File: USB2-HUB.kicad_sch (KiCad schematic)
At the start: 42 parts, among them J4 USB_OTG, U2 TLV71311PDBV, U3 FSUSB42MUX, U4 TUSB4041IPAPQ1, U5 TPD4EUSB30, Y1 24MHz Crystal

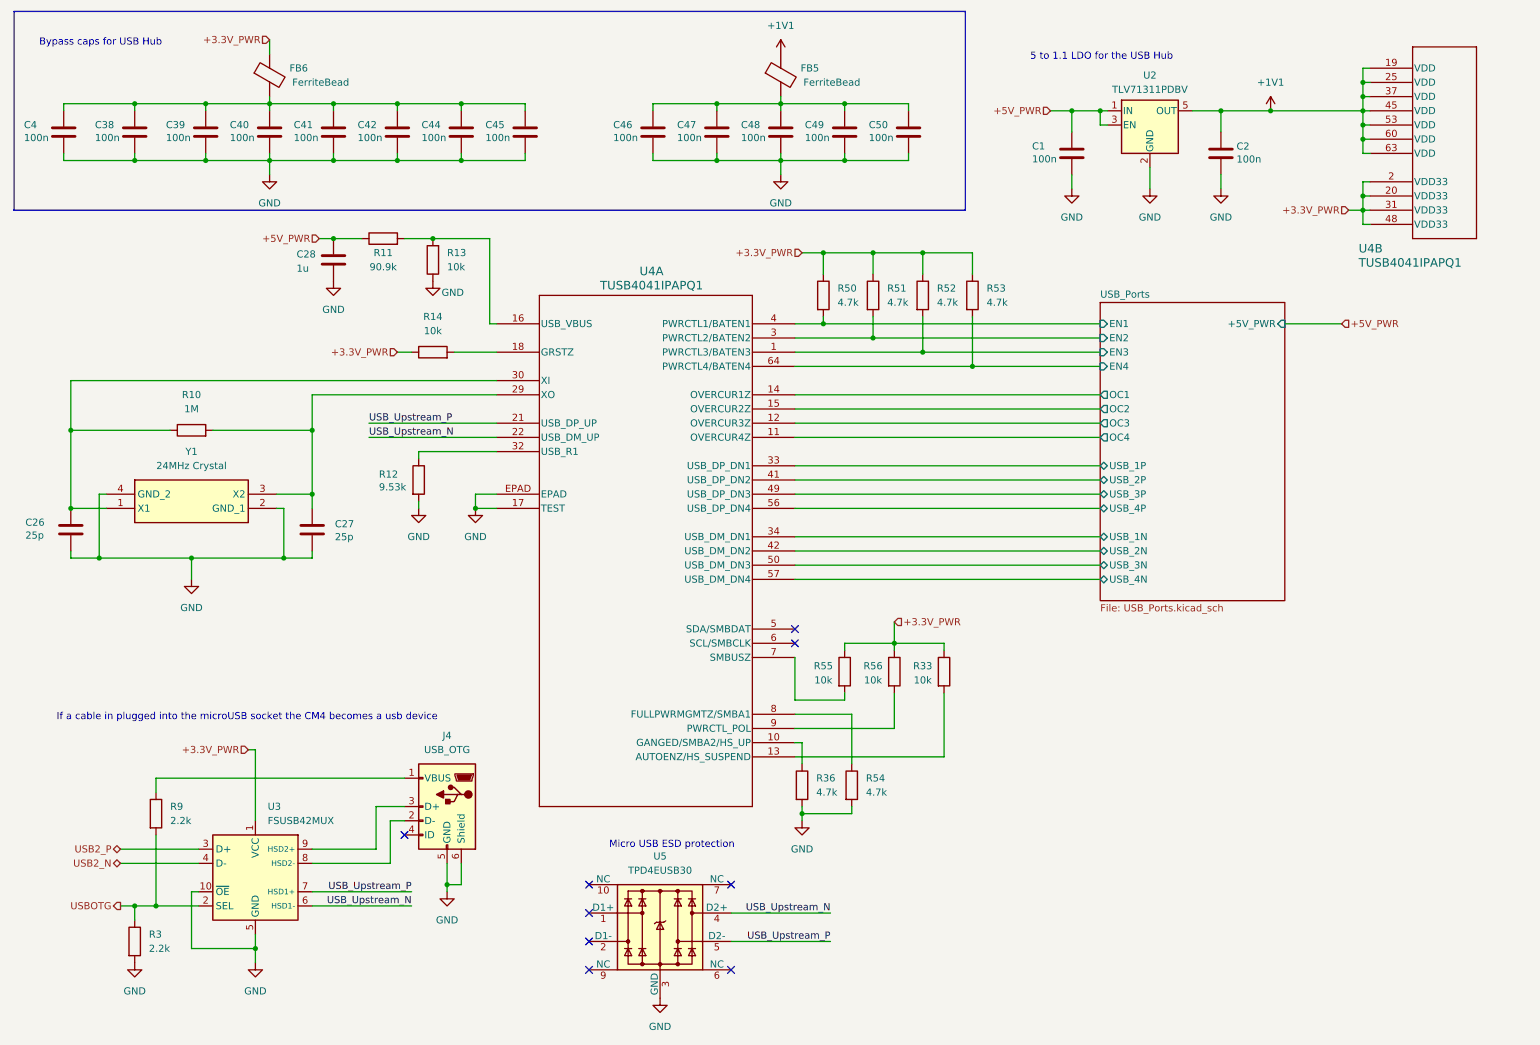
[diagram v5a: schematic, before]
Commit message: Migrate to USB C and added some ESD protections on Vbus; might still have some issues
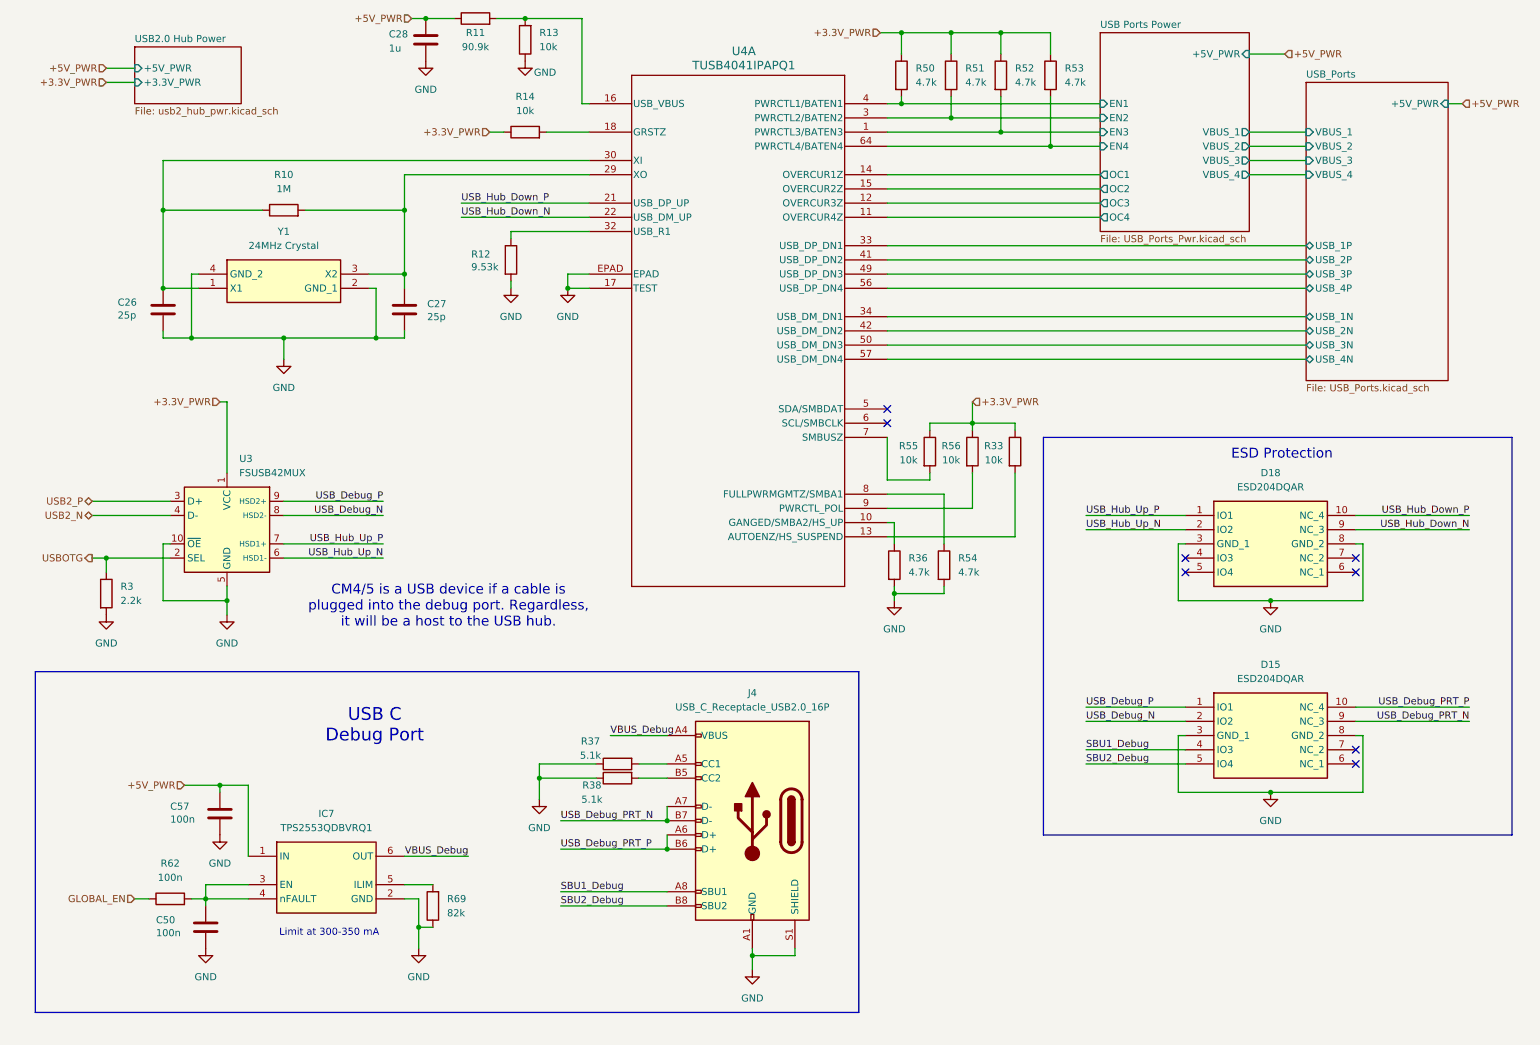
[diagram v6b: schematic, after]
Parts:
- removed C1, C2, C38, C39, C4, C40, C41, C42, C44, C45, C46, C47, C48, C49: 100n, Capacitor_SMD:C_0805_2012Metric, symbol Device:C
- removed FB5, FB6: FerriteBead, Inductor_SMD:L_1206_3216Metric, symbol Device:FerriteBead
- removed J4: USB_OTG, Connector_USB:USB_Micro-B_Molex-105017-0001, symbol Connector:USB_OTG
- removed R9: 2.2k, Resistor_SMD:R_0805_2012Metric, symbol Device:R
- removed U2: TLV71311PDBV, Package_TO_SOT_SMD:SOT-23-5, symbol Regulator_Linear:TLV71311PDBV
- removed unit 2 of U4
- removed U5: TPD4EUSB30, Package_SON:USON-10_2.5x1.0mm_P0.5mm, symbol Power_Protection:TPD4EUSB30
- added C57: 100n, Capacitor_SMD:C_0805_2012Metric, symbol Device:C
- added D15, D18: ESD204DQAR, Controls_Pi:ESD204DQAR, symbol ESD204DQAR:ESD204DQAR
- added IC7: TPS2553QDBVRQ1, Controls_Pi:SOT95P280X145-6N, symbol TPS2553QDBVRQ1:TPS2553QDBVRQ1
- added J4: USB_C_Receptacle_USB2.0_16P, symbol Connector:USB_C_Receptacle_USB2.0_16P
- added R37, R38: 5.1k, Resistor_SMD:R_0805_2012Metric, symbol Device:R
- added R62: 100n, Resistor_SMD:R_0805_2012Metric, symbol Device:R
- added R69: 82k, Resistor_SMD:R_0805_2012Metric, symbol Device:R
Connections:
- net +5V_PWR: now also C57.1, IC7.1 (IN)
- net GND: now also C57.2, D15.3 (GND_1), D15.8 (GND_2), D18.3 (GND_1), D18.8 (GND_2), IC7.2 (GND), J4.A1 (GND), J4.A12 (GND), J4.B1 (GND), J4.B12 (GND), J4.S1 (SHIELD), R37.1, R38.1, R69.1
- net at C50.1: now also IC7.3 (EN), IC7.4 (nFAULT), R62.2
- net USB_Debug_N: now reaches U3.8 (HSD2-)
- net USB_Debug_N: now also D15.2 (IO2)
- net USB_Debug_P: now reaches U3.9 (HSD2+)
- net USB_Debug_P: now also D15.1 (IO1)
- net USB_Ports/EN1 renamed USB Ports Power/EN1
- net USB_Ports/EN2 renamed USB Ports Power/EN2
- net USB_Ports/EN3 renamed USB Ports Power/EN3
- net USB_Ports/EN4 renamed USB Ports Power/EN4
- net USB_Ports/OC1 renamed USB Ports Power/OC1
- net USB_Ports/OC2 renamed USB Ports Power/OC2
- net USB_Ports/OC3 renamed USB Ports Power/OC3
- net USB_Ports/OC4 renamed USB Ports Power/OC4
- net USB_Upstream_N renamed USB_Hub_Down_N
- net USB_Hub_Down_N: now also D18.9 (NC_3); no longer U3.6 (HSD1-)
- net USB_Upstream_P renamed USB_Hub_Down_P
- net USB_Hub_Down_P: now also D18.10 (NC_4); no longer U3.7 (HSD1+)
- new net: J4.A5 (CC1), R37.2
- new net: IC7.5 (ILIM), R69.2
- new net: J4.B5 (CC2), R38.2
- new net GLOBAL_EN: R62.1
- new net SBU1_Debug: D15.4 (IO3), J4.A8 (SBU1)
- new net SBU2_Debug: D15.5 (IO4), J4.B8 (SBU2)
- new net USB_Debug_PRT_N: D15.9 (NC_3), J4.A7 (D-), J4.B7 (D-)
- new net USB_Debug_PRT_P: D15.10 (NC_4), J4.A6 (D+), J4.B6 (D+)
- new net USB_Hub_Up_N: D18.2 (IO2), U3.6 (HSD1-)
- new net USB_Hub_Up_P: D18.1 (IO1), U3.7 (HSD1+)
- new net VBUS_Debug: IC7.6 (OUT), J4.A4 (VBUS), J4.A9 (VBUS), J4.B4 (VBUS), J4.B9 (VBUS)
- no-connect marks 9 -> 8
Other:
- added sheet USB Ports Power (USB_Ports_Pwr.kicad_sch)
- added sheet USB2.0 Hub Power (usb2_hub_pwr.kicad_sch)
- sheet USB_Ports ports: added VBUS_1, VBUS_2, VBUS_3, VBUS_4; removed EN1, EN2, EN3, EN4, OC1, OC2, OC3, OC4
- note added: "CM4/5 is a USB device if a cable is plugged into the debug port. Regardless, it will be a host to the USB hub."
- note added: "ESD Protection"
- note added: "Limit at 300-350 mA"
- note added: "USB C Debug Port"
- note removed: "5 to 1.1 LDO for the USB Hub"
- note removed: "Bypass caps for USB Hub"
- note removed: "If a cable in plugged into the microUSB socket the CM4 becomes a usb device"
- note removed: "Micro USB ESD protection"
- moved on the sheet: C26, C27, C28, R10, R11, R12, R13, R14, R3, R33, R36, R50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

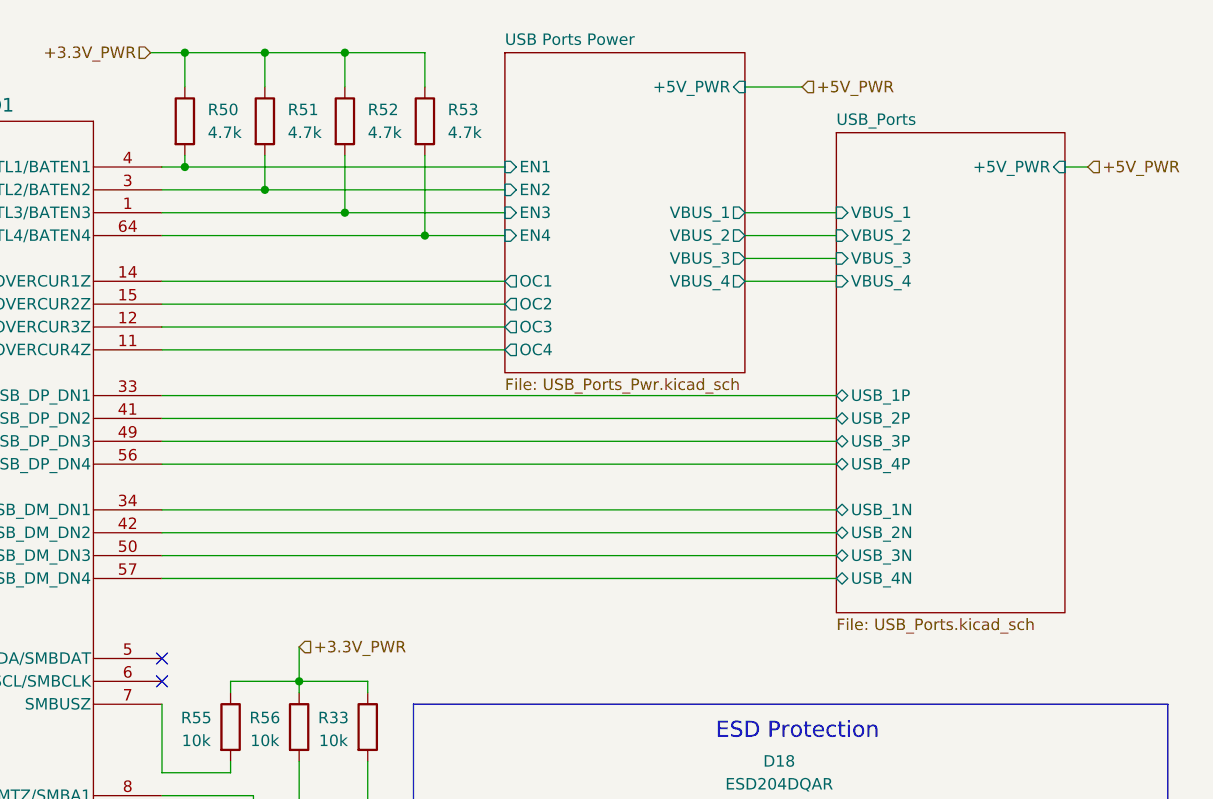
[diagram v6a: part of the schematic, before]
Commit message: fixed erc and removed old schematics
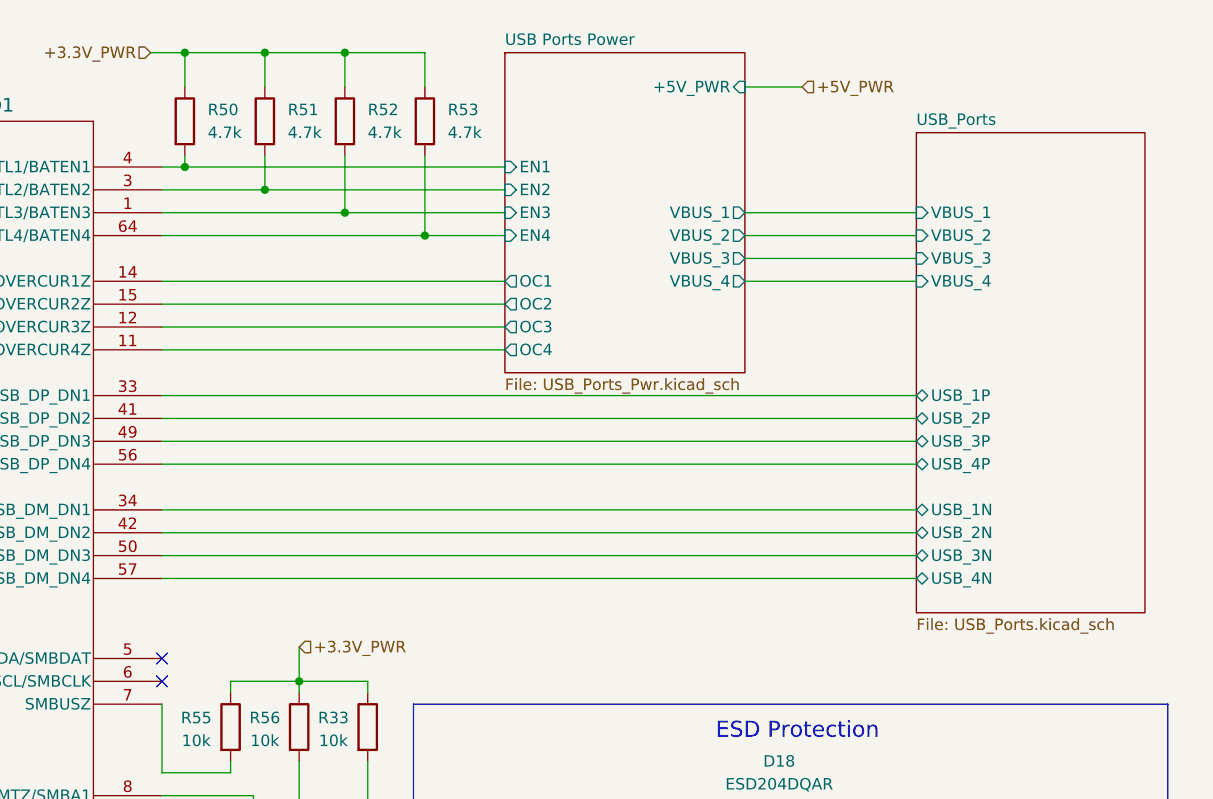
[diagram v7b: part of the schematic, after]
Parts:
- D15, D18: Arrow Part Number (none) -> ESD204DQAR; Arrow Price/Stock (none) -> https://www.arrow.com/en/products/esd204dqar/texas-instrume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; Height (none) -> 0.55; Manufacturer_Name (none) -> Texas Instruments; Manufacturer_Part_Number (none) -> ESD204DQAR; Mouser Part Number (none) -> 595-ESD204DQAR; Mouser Price/Stock (none) -> https://www.mouser.co.uk/ProductDetail/Texas-Instruments/ES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
- IC7: Arrow Part Number (none) -> TPS2553QDBVRQ1; Arrow Price/Stock (none) -> https://www.arrow.com/en/products/tps2553qdbvrq1/texas-inst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; Height (none) -> 1.45; Manufacturer_Name (none) -> Texas Instruments; Manufacturer_Part_Number (none) -> TPS2553QDBVRQ1; Mouser Part Number (none) -> 595-TPS2553QDBVRQ1; Mouser Price/Stock (none) -> https://www.mouser.co.uk/ProductDetail/Texas-Instruments/TP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
- Y1: Height (none) -> 0.8; Manufacturer_Name (none) -> ABRACON; Manufacturer_Part_Number (none) -> ABM8AIG-24.000MHZ-12-2Z-T3; Mouser Part Number (none) -> 815-M8AIG-24-12-2ZT3; Mouser Price/Stock (none) -> https://www.mouser.co.uk/ProductDetail/ABRACON/ABM8AIG-2400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
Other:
- sheet USB_Ports ports: added none; removed +5V_PWR
